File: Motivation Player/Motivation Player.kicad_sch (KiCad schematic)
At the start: 0 parts

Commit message: PCB Design
Wired and designed some of the core functionalities. Looking into how to wire the audio amplifier and what type to use
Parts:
- added A1: RaspberryPi_Pico, Module:RaspberryPi_Pico_Common_Unspecified, symbol MCU_Module:RaspberryPi_Pico
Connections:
- new net: A1.13 (GND), A1.18 (GND), A1.23 (GND), A1.28 (GND), A1.3 (GND), A1.38 (GND), A1.8 (GND)
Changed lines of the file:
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@@
 	(generator_version "9.0")
 	(paper "A4")
+	(symbol
+		(lib_id "MCU_Module:RaspberryPi_Pico")
+		(at 186.69 102.87 0)
+		(unit 1)
+		(exclude_from_sim no)
+		(in_bom yes)
+		(on_board yes)
+		(dnp no)
+		(fields_autoplaced yes)
+		(property "Reference" "A1"
+			(at 188.8333 137.16 0)
+			(effects
+				(font
+					(size 1.27 1.27)
+				)
+				(justify left)
+			)
+		)
+		(property "Value" "RaspberryPi_Pico"
+			(at 188.8333 139.7 0)
+			(effects
+				(font
+					(size 1.27 1.27)
+				)
+				(justify left)
+			)
+		)
+		(property "Footprint" "Module:RaspberryPi_Pico_Common_Unspecified"
+			(at 186.69 149.86 0)
+			(effects
+				(font
+					(size 1.27 1.27)
+				)
+				(hide yes)
+			)
+		)
+		(property "Datasheet" "https://datasheets.raspberrypi.com/pico/pico-datasheet.pdf"
+			(at 186.69 152.4 0)
+			(effects
+				(font
+					(size 1.27 1.27)
+				)
+				(hide yes)
+			)
+		)
+		(property "Description" "Versatile and inexpensive microcontroller module powered by RP2040 dual-core Arm Cortex-M0+ processor up to 133 MHz, 264kB SRAM, 2MB QSPI flash; also supports Raspberry Pi Pico 2"
+			(at 186.69 154.94 0)
+			(effects
+				(font
+					(size 1.27 1.27)
+				)
+				(hide yes)
+			)
+		)
+		(pin "15"
+		)
+		(pin "9"
+		)
+		(pin "8"
+		)
+		(pin "23"
+		)
+		(pin "30"
+		)
+		(pin "17"
+		)
+		(pin "38"
+		)
+		(pin "4"
+		)
+		(pin "37"
+		)
+		(pin "5"
+		)
+		(pin "10"
+		)
+		(pin "11"
+		)
+		(pin "14"
+		)
+		(pin "20"
+		)
+		(pin "39"
+		)
+		(pin "6"
+		)
+		(pin "7"
+		)
+		(pin "12"
+		)
+		(pin "13"
+		)
+		(pin "1"
+		)
+		(pin "16"
+		)
+		(pin "18"
+		)
+		(pin "3"
+		)
+		(pin "19"
+		)
+		(pin "2"
+		)
+		(pin "28"
+		)
+		(pin "40"
+		)
+		(pin "25"
+		)
+		(pin "33"
+		)
+		(pin "31"
+		)
+		(pin "24"
+		)
+		(pin "27"
+		)
+		(pin "21"
+		)
+		(pin "29"
+		)
+		(pin "35"
+		)
+		(pin "36"
+		)
+		(pin "26"
+		)
+		(pin "34"
+		)
+		(pin "32"
+		)
+		(pin "22"
+		)
+		(instances
+			(project ""
+				(path "/8edc0c1b-df8d-45ab-9d77-b739dad39e61"
+					(reference "A1")
+					(unit 1)
+				)
+			)
+		)
+	)
 	(sheet_instances
 		(path "/"

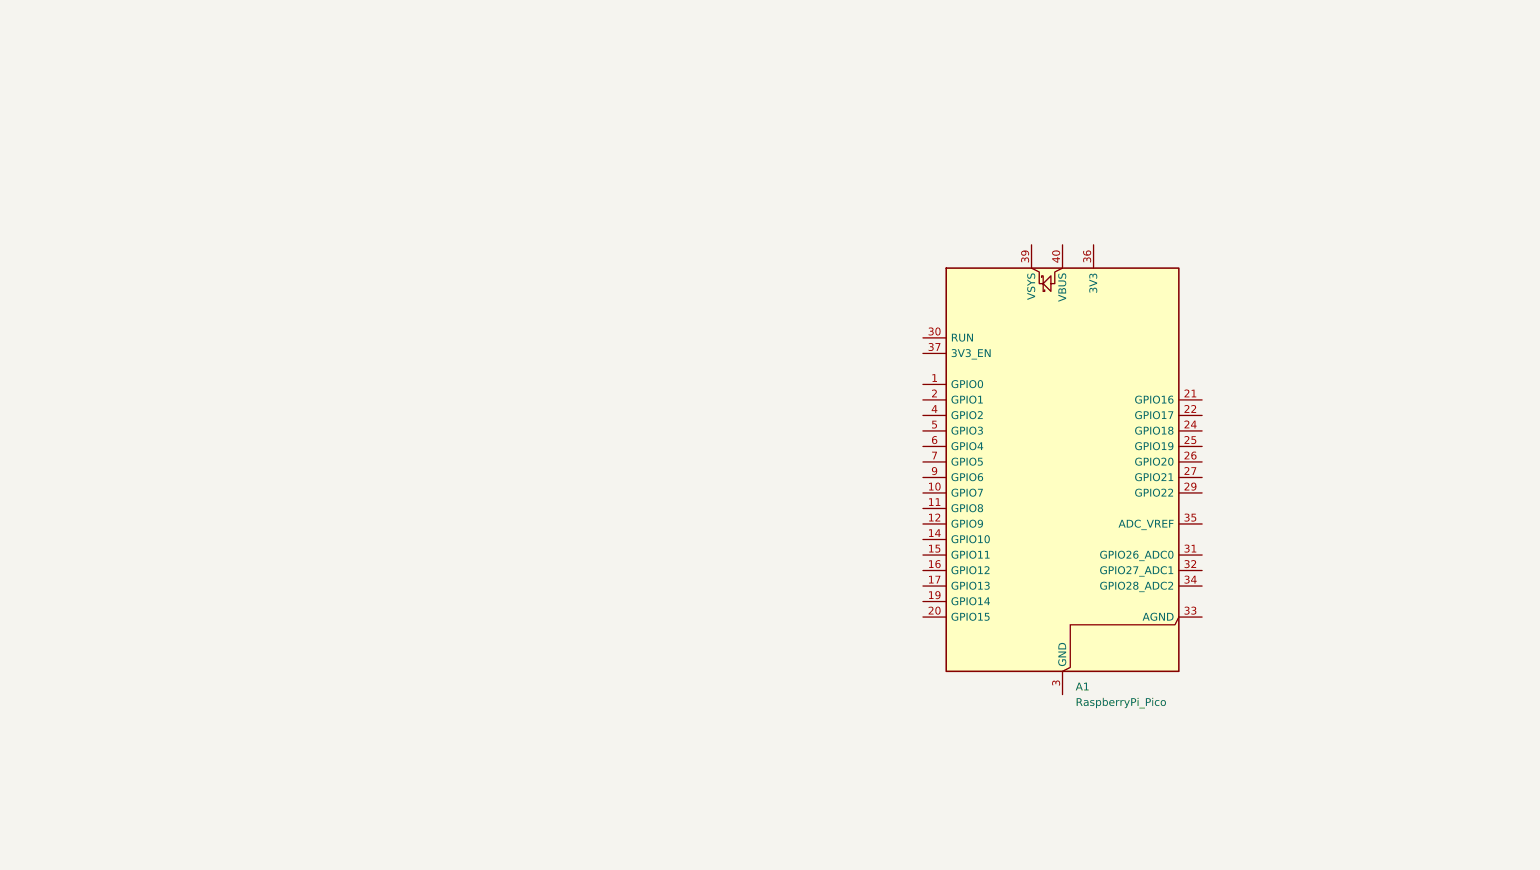
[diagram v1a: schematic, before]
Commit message: PCB Schematic and Footprints
Finished the PCB schematic and assigned the footprints
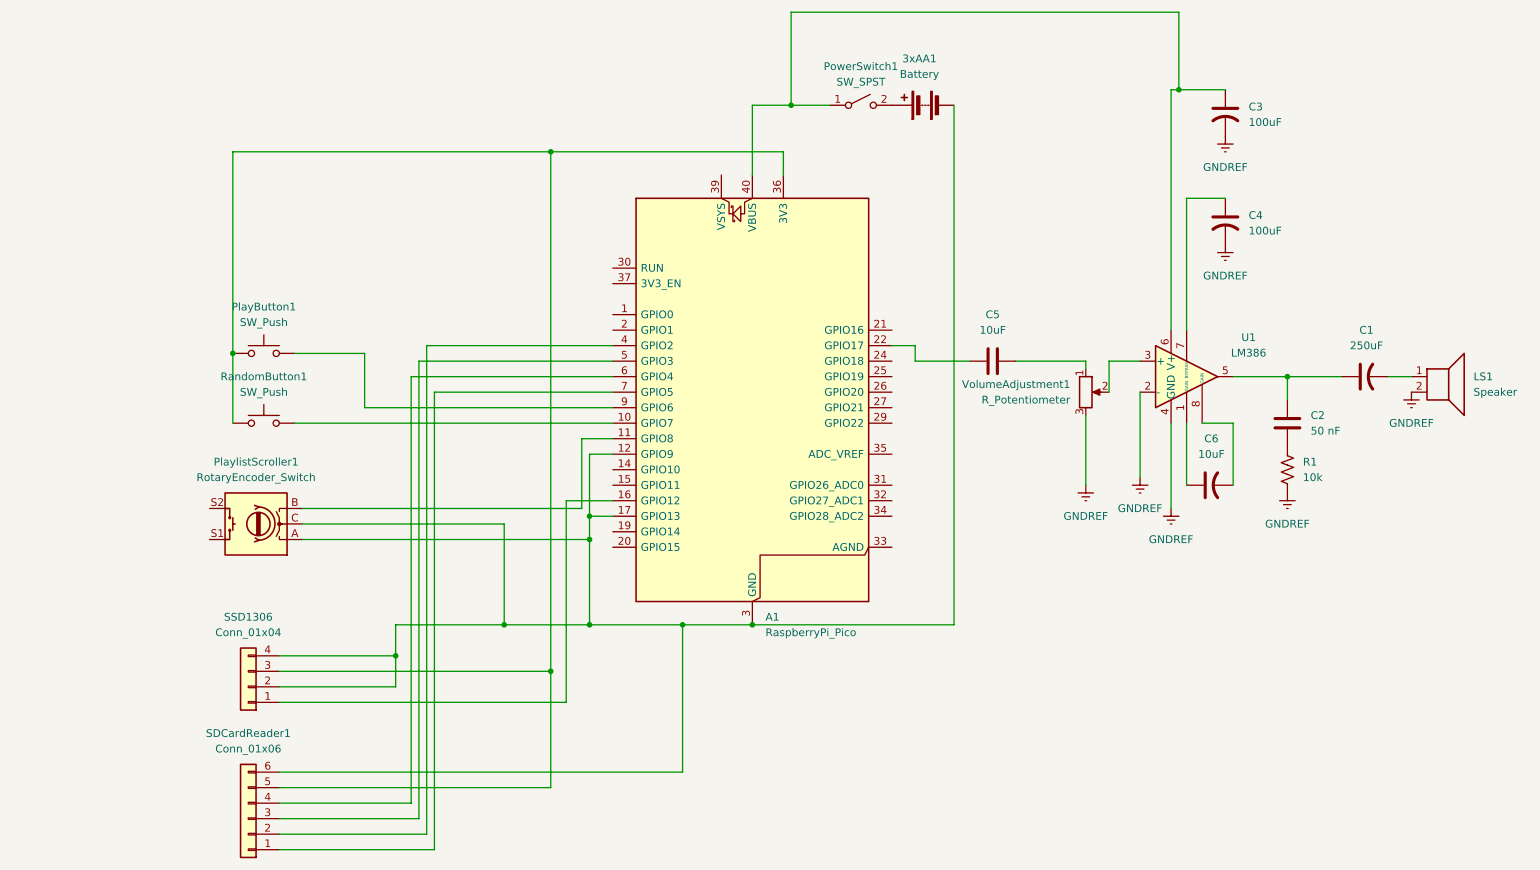
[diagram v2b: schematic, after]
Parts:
- added 3xAA1: Battery, Battery:BatteryHolder_TruPower_BH-331P_3xAA, symbol Device:Battery
- added C1: 250uF, Capacitor_THT:CP_Radial_D6.3mm_P2.50mm, symbol Device:C_US
- added C2: 50 nF, Capacitor_THT:C_Disc_D5.0mm_W2.5mm_P5.00mm, symbol Device:C
- added C3, C4: 100uF, Capacitor_THT:CP_Radial_D5.0mm_P2.50mm, symbol Device:C_US
- added C5: 10uF, Capacitor_THT:CP_Radial_D5.0mm_P2.50mm, symbol Device:C
- added C6: 10uF, Capacitor_THT:CP_Radial_D5.0mm_P2.50mm, symbol Device:C_US
- added LS1: Speaker, Connector_Wire:SolderWire-0.1sqmm_1x02_P3.6mm_D0.4mm_OD1mm_Relief, symbol Device:Speaker
- added PlayButton1, RandomButton1: SW_Push, Button_Switch_THT:SW_PUSH-12mm, symbol Switch:SW_Push
- added PlaylistScroller1: RotaryEncoder_Switch, Rotary_Encoder:RotaryEncoder_Alps_EC11E-Switch_Vertical_H20mm, symbol Device:RotaryEncoder_Switch
- added PowerSwitch1: SW_SPST, Connector_Wire:SolderWire-0.1sqmm_1x02_P3.6mm_D0.4mm_OD1mm_Relief, symbol Switch:SW_SPST
- added R1: 10k, Resistor_THT:R_Axial_DIN0207_L6.3mm_D2.5mm_P10.16mm_Horizontal, symbol Device:R_US
- added SDCardReader1: Conn_01x06, Connector_PinHeader_1.27mm:PinHeader_1x06_P1.27mm_Vertical, symbol Connector_Generic:Conn_01x06
- added SSD1306: Conn_01x04, Connector_PinHeader_1.27mm:PinHeader_1x04_P1.27mm_Vertical, symbol Connector_Generic:Conn_01x04
- added U1: LM386, Package_DIP:DIP-8_W7.62mm_Socket, symbol Amplifier_Audio:LM386
- added VolumeAdjustment1: R_Potentiometer, Potentiometer_THT:Potentiometer_Piher_PT-10-V10_Vertical, symbol Device:R_Potentiometer
- A1: footprint Module:RaspberryPi_Pico_Common_Unspecified -> Module:RaspberryPi_Pico_Common_THT
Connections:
- net at A1.10 (GPIO7): now also RandomButton1.2
- net at A1.11 (GPIO8): now also PlaylistScroller1.B
- net at A1.12 (GPIO9): now also A1.13 (GND), A1.17 (GPIO13), A1.18 (GND), A1.23 (GND), A1.28 (GND), A1.3 (GND), A1.38 (GND), A1.8 (GND), 3xAA1.2 (-), PlaylistScroller1.A, PlaylistScroller1.C, SDCardReader1.6 (Pin_6), SSD1306.2 (Pin_2), SSD1306.4 (Pin_4)
- net at A1.16 (GPIO12): now also SSD1306.1 (Pin_1)
- net at A1.22 (GPIO17): now also C5.1
- net at A1.36 (3V3): now also PlayButton1.1, RandomButton1.1, SDCardReader1.5 (Pin_5), SSD1306.3 (Pin_3)
- net at A1.4 (GPIO2): now also SDCardReader1.2 (Pin_2)
- net at A1.40 (VBUS): now also C3.1, PowerSwitch1.1 (A), U1.6 (V+)
- net at A1.5 (GPIO3): now also SDCardReader1.3 (Pin_3)
- net at A1.6 (GPIO4): now also SDCardReader1.4 (Pin_4)
- net at A1.7 (GPIO5): now also SDCardReader1.1 (Pin_1)
- net at A1.9 (GPIO6): now also PlayButton1.2
- new net: C1.1, C2.1, U1.5
- new net: C1.2, LS1.1
- new net: 3xAA1.1 (+), PowerSwitch1.2 (B)
- new net: C2.2, R1.1
- new net: C5.2, VolumeAdjustment1.1
- new net: U1.3 (+), VolumeAdjustment1.2
- new net: C6.1, U1.1 (GAIN)
- new net: C6.2, U1.8 (GAIN)
- new net: C4.1, U1.7 (BYPASS)
- new net GNDREF: C3.2, C4.2, LS1.2, R1.2, U1.2 (-), U1.4 (GND), VolumeAdjustment1.3
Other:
- moved on the sheet: A1

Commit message: Finishing up PCB
Finished up PCB design
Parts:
- removed PlaylistScroller1: RotaryEncoder_Switch, Rotary_Encoder:RotaryEncoder_Alps_EC11E-Switch_Vertical_H20mm, symbol Device:RotaryEncoder_Switch
- added PlaylistScroller1: RotaryEncoder_Switch_MP, Rotary_Encoder:RotaryEncoder_Alps_EC11E-Switch_Vertical_H20mm, symbol Device:RotaryEncoder_Switch_MP
- SDCardReader1: footprint Connector_PinHeader_1.27mm:PinHeader_1x06_P1.27mm_Vertical -> Connector_PinHeader_2.54mm:PinHeader_1x06_P2.54mm_Vertical
- SSD1306: footprint Connector_PinHeader_1.27mm:PinHeader_1x04_P1.27mm_Vertical -> Connector_PinHeader_2.54mm:PinHeader_1x04_P2.54mm_Vertical
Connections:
- net GNDREF: now also 3xAA1.2 (-), A1.13 (GND), A1.18 (GND), A1.23 (GND), A1.28 (GND), A1.3 (GND), A1.38 (GND), A1.8 (GND), PlayButton1.1, RandomButton1.1, SDCardReader1.6 (Pin_6), SSD1306.1 (Pin_1), PlaylistScroller1.C, PlaylistScroller1.MP
- net at A1.7 (GPIO5): now also SDCardReader1.2 (Pin_2); no longer SDCardReader1.1 (Pin_1)
- net at A1.4 (GPIO2): now also SDCardReader1.4 (Pin_4); no longer SDCardReader1.2 (Pin_2)
- net at A1.6 (GPIO4): now also SDCardReader1.5 (Pin_5); no longer SDCardReader1.4 (Pin_4)
- net at A1.11 (GPIO8): now also PlaylistScroller1.B
- net at A1.16 (GPIO12): now also SSD1306.4 (Pin_4); no longer SSD1306.1 (Pin_1)
- new net: A1.12 (GPIO9), PlaylistScroller1.A
- new net: A1.17 (GPIO13), SSD1306.3 (Pin_3)
- new net +3.3V: A1.36 (3V3), SDCardReader1.1 (Pin_1), SSD1306.2 (Pin_2)
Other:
- moved on the sheet: SDCardReader1, SSD1306
